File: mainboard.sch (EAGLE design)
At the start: 17 parts, among them IC1 7805TV, IC2 7805TV, IC3 7805TV, X1 22-23-2021

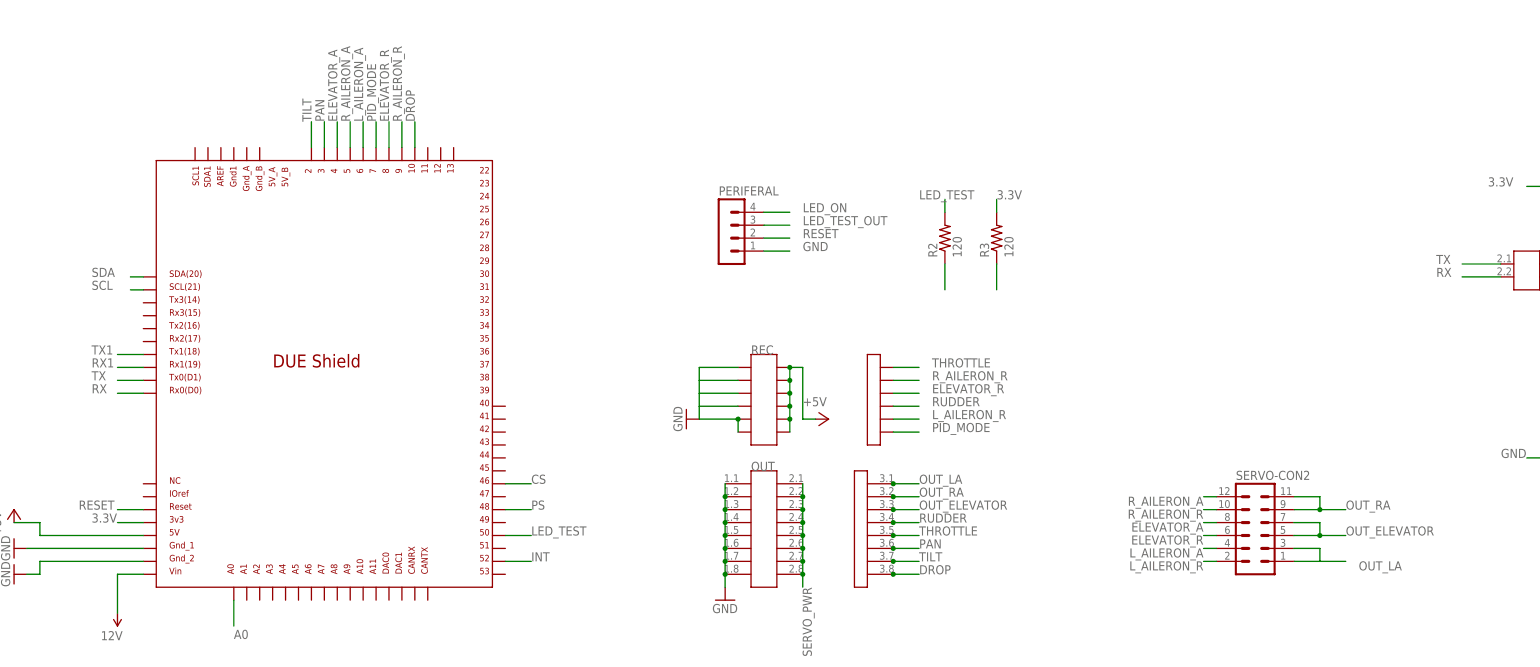
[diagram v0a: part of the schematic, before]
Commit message: Fix servo connections and remove unnecessary parts
changes from Schindeler's feedback
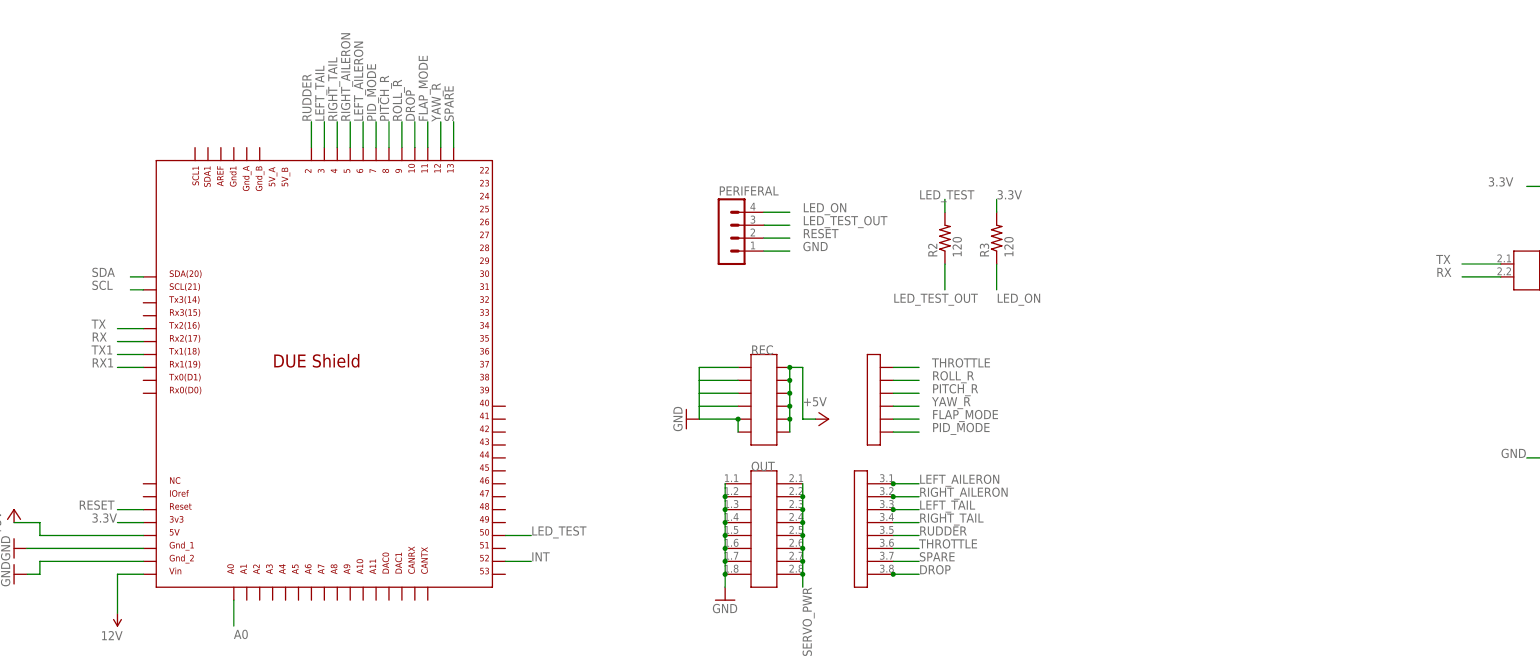
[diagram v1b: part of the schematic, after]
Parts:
- removed SERVO-CON2: (no value), con-lstb:MA06-2
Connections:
- removed net CS: U$1.46
- removed net ELEVATOR_A: SERVO-CON2.8, U$1.4
- removed net ELEVATOR_R: REC.3.3, SERVO-CON2.6, U$1.8
- removed net L_AILERON_A: SERVO-CON2.4, U$1.6
- removed net L_AILERON_R: REC.3.5, SERVO-CON2.2
- removed net OUT_ELEVATOR: OUT.3.3, SERVO-CON2.5, SERVO-CON2.7
- removed net OUT_LA: OUT.3.1, SERVO-CON2.1, SERVO-CON2.3
- removed net OUT_RA: OUT.3.2, SERVO-CON2.11, SERVO-CON2.9
- removed net PAN: OUT.3.6, U$1.3
- removed net PS: U$1.48
- removed net R_AILERON_A: SERVO-CON2.12, U$1.5
- removed net R_AILERON_R: REC.3.2, SERVO-CON2.10, U$1.9
- removed net TILT: OUT.3.7, U$1.2
- new net FLAP_MODE: REC.3.5, U$1.11
- new net LEFT_AILERON: OUT.3.1, U$1.6
- new net LEFT_TAIL: OUT.3.3, U$1.3
- new net PITCH_R: REC.3.3, U$1.8
- new net RIGHT_AILERON: OUT.3.2, U$1.5
- new net RIGHT_TAIL: OUT.3.4, U$1.4
- new net ROLL_R: REC.3.2, U$1.9
- new net SPARE: OUT.3.7, U$1.13
- new net YAW_R: REC.3.4, U$1.12
- net RUDDER: now also OUT.3.5, U$1.2; no longer OUT.3.4, REC.3.4
- net RX: now also U$1.RX2; no longer U$1.RX0
- net THROTTLE: now also OUT.3.6; no longer OUT.3.5
- net TX: now also U$1.TX2; no longer U$1.TX0

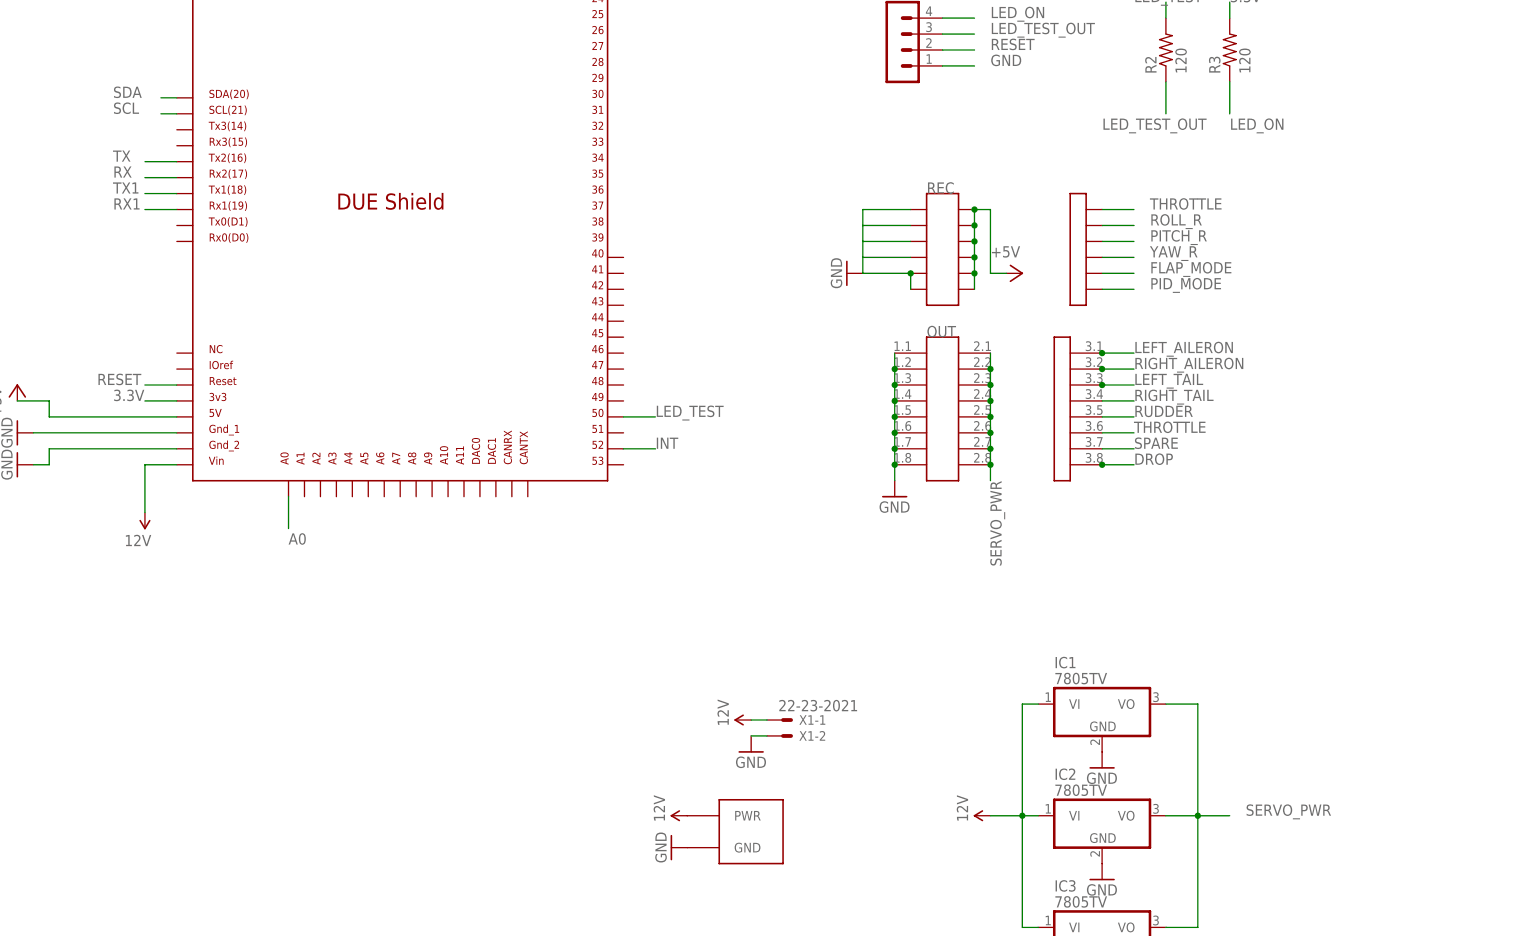
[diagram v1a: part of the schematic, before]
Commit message: Update labels on board and servo connections
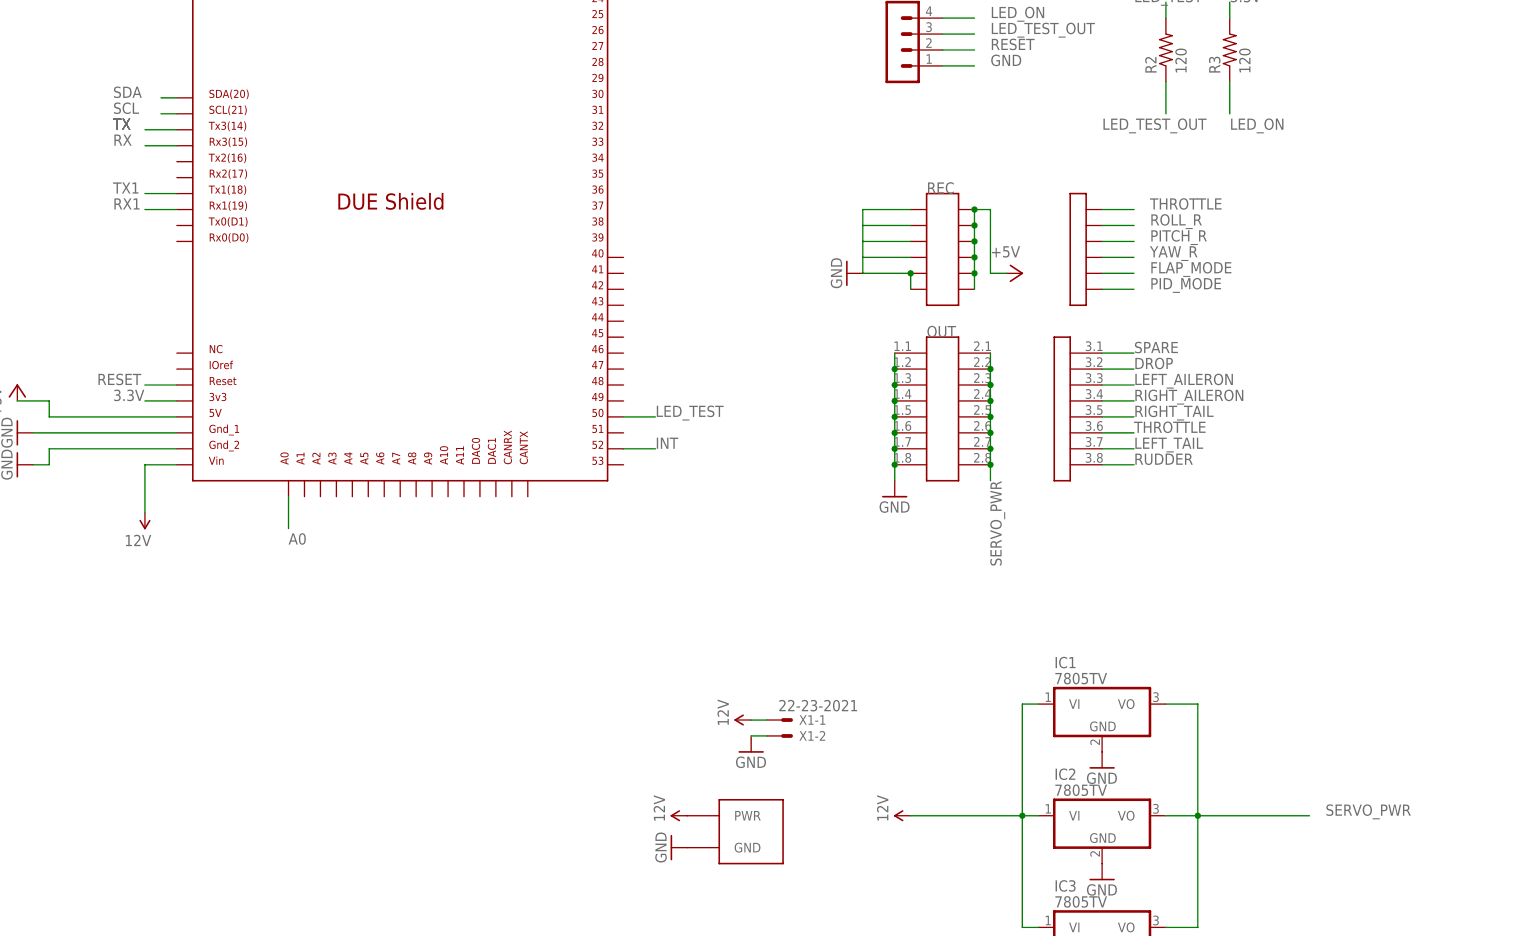
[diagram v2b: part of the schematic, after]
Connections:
- net DROP: now also OUT.3.2; no longer OUT.3.8
- net LEFT_AILERON: now also OUT.3.3; no longer OUT.3.1
- net LEFT_TAIL: now also OUT.3.7; no longer OUT.3.3
- net RIGHT_AILERON: now also OUT.3.4; no longer OUT.3.2
- net RIGHT_TAIL: now also OUT.3.5; no longer OUT.3.4
- net RUDDER: now also OUT.3.8; no longer OUT.3.5
- net RX: now also U$1.RX3; no longer U$1.RX2
- net SPARE: now also OUT.3.1; no longer OUT.3.7
- net TX: now also U$1.TX3; no longer U$1.TX2
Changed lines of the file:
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@@
 <instance part="IC2" gate="A1" x="195.58" y="-35.56"/>
 <instance part="IC3" gate="A1" x="195.58" y="-53.34"/>
-<instance part="SUPPLY2" gate="G$1" x="177.8" y="-35.56" rot="R90"/>
+<instance part="SUPPLY2" gate="G$1" x="165.1" y="-35.56" rot="R90"/>
 <instance part="GND8" gate="1" x="195.58" y="-27.94"/>
 <instance part="GND10" gate="1" x="195.58" y="-45.72"/>
@@
 <net name="LEFT_AILERON" class="0">
 <segment>
-<wire x1="195.58" y1="38.1" x2="200.66" y2="38.1" width="0.1524" layer="91"/>
-<label x="200.66" y="38.1" size="1.778" layer="95"/>
-<pinref part="OUT" gate="G$1" pin="3.1"/>
-<junction x="195.58" y="38.1"/>
-</segment>
-<segment>
 <pinref part="U$1" gate="G$1" pin="6"/>
 <wire x1="91.44" y1="104.14" x2="91.44" y2="109.22" width="0.1524" layer="91"/>
 <label x="91.44" y="109.22" size="1.778" layer="95" rot="R90"/>
 </segment>
+<segment>
+<pinref part="OUT" gate="G$1" pin="3.3"/>
+<wire x1="195.58" y1="33.02" x2="200.66" y2="33.02" width="0.1524" layer="91"/>
+<label x="200.66" y="33.02" size="1.778" layer="95"/>
+</segment>
 </net>
 <net name="RIGHT_AILERON" class="0">
-<segment>
-<wire x1="195.58" y1="35.56" x2="200.66" y2="35.56" width="0.1524" layer="91"/>
-<label x="200.66" y="35.56" size="1.778" layer="95"/>
-<pinref part="OUT" gate="G$1" pin="3.2"/>
-<junction x="195.58" y="35.56"/>
-</segment>
 <segment>
 <pinref part="U$1" gate="G$1" pin="5"/>
@@
 <label x="88.9" y="109.22" size="1.778" layer="95" rot="R90"/>
 </segment>
+<segment>
+<pinref part="OUT" gate="G$1" pin="3.4"/>
+<wire x1="195.58" y1="30.48" x2="200.66" y2="30.48" width="0.1524" layer="91"/>
+<label x="200.66" y="30.48" size="1.778" layer="95"/>
+</segment>
 </net>
 <net name="ROLL_R" class="0">
@@
 </segment>
 <segment>
-<pinref part="OUT" gate="G$1" pin="3.4"/>
-<wire x1="195.58" y1="30.48" x2="200.66" y2="30.48" width="0.1524" layer="91"/>
-<label x="200.66" y="30.48" size="1.778" layer="95"/>
+<pinref part="OUT" gate="G$1" pin="3.5"/>
+<wire x1="195.58" y1="27.94" x2="200.66" y2="27.94" width="0.1524" layer="91"/>
+<label x="200.66" y="27.94" size="1.778" layer="95"/>
 </segment>
 </net>
@@
 <wire x1="205.74" y1="-35.56" x2="210.82" y2="-35.56" width="0.1524" layer="91"/>
 <junction x="210.82" y="-35.56"/>
-<wire x1="210.82" y1="-35.56" x2="215.9" y2="-35.56" width="0.1524" layer="91"/>
-<label x="218.44" y="-35.56" size="1.778" layer="95"/>
+<wire x1="210.82" y1="-35.56" x2="228.6" y2="-35.56" width="0.1524" layer="91"/>
+<label x="231.14" y="-35.56" size="1.778" layer="95"/>
 </segment>
 </net>
@@
 <pinref part="IC1" gate="A1" pin="VI"/>
 <wire x1="182.88" y1="-17.78" x2="185.42" y2="-17.78" width="0.1524" layer="91"/>
-<wire x1="182.88" y1="-35.56" x2="177.8" y2="-35.56" width="0.1524" layer="91"/>
+<wire x1="182.88" y1="-35.56" x2="165.1" y2="-35.56" width="0.1524" layer="91"/>
 <pinref part="SUPPLY2" gate="G$1" pin="12V"/>
 <pinref part="IC2" gate="A1" pin="VI"/>
@@
 </segment>
 <segment>
-<pinref part="U$1" gate="G$1" pin="TX2"/>
-<wire x1="48.26" y1="68.58" x2="43.18" y2="68.58" width="0.1524" layer="91"/>
-<label x="38.1" y="68.58" size="1.778" layer="95"/>
+<pinref part="U$1" gate="G$1" pin="TX3"/>
+<wire x1="48.26" y1="73.66" x2="43.18" y2="73.66" width="0.1524" layer="91"/>
+<label x="38.1" y="73.66" size="1.778" layer="95"/>
+<label x="38.1" y="73.66" size="1.778" layer="95"/>
+<label x="38.1" y="73.66" size="1.778" layer="95"/>
 </segment>
 </net>
@@
 </segment>
 <segment>
-<pinref part="U$1" gate="G$1" pin="RX2"/>
-<wire x1="48.26" y1="66.04" x2="43.18" y2="66.04" width="0.1524" layer="91"/>
-<label x="38.1" y="66.04" size="1.778" layer="95"/>
+<pinref part="U$1" gate="G$1" pin="RX3"/>
+<wire x1="48.26" y1="71.12" x2="43.18" y2="71.12" width="0.1524" layer="91"/>
+<label x="38.1" y="71.12" size="1.778" layer="95"/>
 </segment>
 </net>
@@
 <net name="DROP" class="0">
 <segment>
-<pinref part="OUT" gate="G$1" pin="3.8"/>
-<wire x1="195.58" y1="20.32" x2="200.66" y2="20.32" width="0.1524" layer="91"/>
-<junction x="195.58" y="20.32"/>
-<label x="200.66" y="20.32" size="1.778" layer="95"/>
-</segment>
-<segment>
 <pinref part="U$1" gate="G$1" pin="10"/>
 <wire x1="101.6" y1="104.14" x2="101.6" y2="109.22" width="0.1524" layer="91"/>
 <label x="101.6" y="109.22" size="1.778" layer="95" rot="R90"/>
 </segment>
+<segment>
+<pinref part="OUT" gate="G$1" pin="3.2"/>
+<wire x1="195.58" y1="35.56" x2="200.66" y2="35.56" width="0.1524" layer="91"/>
+<label x="200.66" y="35.56" size="1.778" layer="95"/>
+</segment>
 </net>
 <net name="RX1" class="0">
@@
 </segment>
 <segment>
-<wire x1="195.58" y1="33.02" x2="200.66" y2="33.02" width="0.1524" layer="91"/>
-<label x="200.66" y="33.02" size="1.778" layer="95"/>
-<pinref part="OUT" gate="G$1" pin="3.3"/>
-<junction x="195.58" y="33.02"/>
+<pinref part="OUT" gate="G$1" pin="3.7"/>
+<wire x1="195.58" y1="22.86" x2="200.66" y2="22.86" width="0.1524" layer="91"/>
+<label x="200.66" y="22.86" size="1.778" layer="95"/>
 </segment>
 </net>
@@
 </segment>
 <segment>
-<pinref part="OUT" gate="G$1" pin="3.5"/>
-<wire x1="195.58" y1="27.94" x2="200.66" y2="27.94" width="0.1524" layer="91"/>
-<label x="200.66" y="27.94" size="1.778" layer="95"/>
+<pinref part="OUT" gate="G$1" pin="3.8"/>
+<wire x1="195.58" y1="20.32" x2="200.66" y2="20.32" width="0.1524" layer="91"/>
+<label x="200.66" y="20.32" size="1.778" layer="95"/>
 </segment>
 </net>
 <net name="SPARE" class="0">
-<segment>
-<pinref part="OUT" gate="G$1" pin="3.7"/>
-<wire x1="195.58" y1="22.86" x2="200.66" y2="22.86" width="0.1524" layer="91"/>
-<label x="200.66" y="22.86" size="1.778" layer="95"/>
-</segment>
 <segment>
 <pinref part="U$1" gate="G$1" pin="13"/>
@@
 <label x="109.22" y="109.22" size="1.778" layer="95" rot="R90"/>
 </segment>
-</net>
+<segment>
+<pinref part="OUT" gate="G$1" pin="3.1"/>
+<wire x1="195.58" y1="38.1" x2="200.66" y2="38.1" width="0.1524" layer="91"/>
+<label x="200.66" y="38.1" size="1.778" layer="95"/>
+</segment>
+</net>

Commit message: final updates
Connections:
- removed net N$1: U$1.GND_1
- net GND: now also U$1.GND_1
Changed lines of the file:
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@@
 </busses>
 <nets>
-<net name="N$1" class="0">
-<segment>
-<pinref part="U$1" gate="G$1" pin="GND_1"/>
-<wire x1="25.4" y1="25.4" x2="48.26" y2="25.4" width="0.1524" layer="91"/>
-</segment>
-</net>
 <net name="+5V" class="0">
 <segment>
@@
 <wire x1="165.1" y1="48.26" x2="165.1" y2="50.8" width="0.1524" layer="91"/>
 <junction x="165.1" y="50.8"/>
+<junction x="157.48" y="58.42"/>
+<junction x="157.48" y="55.88"/>
+<junction x="157.48" y="53.34"/>
+<junction x="157.48" y="50.8"/>
 </segment>
 <segment>
@@
 <label x="-2.54" y="71.12" size="1.778" layer="95"/>
 </segment>
+<segment>
+<pinref part="U$1" gate="G$1" pin="GND_1"/>
+<wire x1="25.4" y1="25.4" x2="48.26" y2="25.4" width="0.1524" layer="91"/>
+<pinref part="GND1" gate="1" pin="GND"/>
+</segment>
 </net>
